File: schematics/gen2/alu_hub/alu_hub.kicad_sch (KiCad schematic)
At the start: 0 parts

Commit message: feat: alu hub + pcb base not finished yet
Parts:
- added BC1: BusConnector, Connector_PCBEdge:BUS_PCIexpress_x16, symbol cpu816symbols:BusConnector
- added C1, C10, C11, C2, C3, C4, C5, C6, C7, C8, C9: C, Capacitor_SMD:C_0805_2012Metric_Pad1.18x1.45mm_HandSolder, symbol Device:C
- added U1, U6: 74LS574, Package_DIP:DIP-20_W7.62mm_Socket_LongPads, symbol 74xx:74LS574
- added U10, U3, U9: 74LS02, Package_DIP:DIP-14_W7.62mm_Socket_LongPads, symbol 74xx:74LS02
- added U2, U7, U8: 74LS245, Package_DIP:DIP-20_W7.62mm_Socket_LongPads, symbol 74xx:74LS245
- added U4, U5: 74LS181, Package_DIP:DIP-24_W15.24mm_Socket_LongPads, symbol 74xx:74LS181
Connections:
- new net: U9.10, U9.11
- new net: U10.10, U9.12
- new net: U10.11, U10.12, U9.13
- new net: U3.4, U6.11 (Cp)
- new net: BC1.A20 (~{LARGL}), U3.5
- new net: BC1.B73 (~{CLK}), U3.3, U3.6
- new net: U10.1, U10.8
- new net: U10.4, U10.9
- new net: BC1.A62 (ALUSO), U5.13 (F3), U8.11 (B7), U9.6
- new net: U5.11 (F2), U8.12 (B6), U9.5
- new net: U5.10 (F1), U8.13 (B5), U9.3
- new net: U5.9 (F0), U8.14 (B4), U9.2
- new net: U10.6, U4.13 (F3), U8.15 (B3)
- new net: U10.5, U4.11 (F2), U8.16 (B2)
- new net: U10.3, U4.10 (F1), U8.17 (B1)
- new net: U10.2, U4.9 (F0), U8.18 (B0)
- new net: BC1.B30 (~{RALU}), U8.19 (CE)
- new net: U9.4, U9.9
- new net: BC1.B20 (~{RARGL}), U7.19 (CE)
- new net: BC1.A19 (~{LARGH}), U3.2
- new net: BC1.A60 (ALUZO), U10.13
- new net: BC1.A61 (~{ALUCO}), U5.16 (Cn+4)
- new net: BC1.B19 (~{RARGH}), U2.19 (CE)
- new net: BC1.B37 (ALUM), U4.8 (M), U5.8 (M)
- new net: BC1.B38 (~{ALUCI}), U4.7 (Cn)
- new net: BC1.B48 (ALUS0), U4.6 (S0), U5.6 (S0)
- new net: BC1.B49 (ALUS1), U4.5 (S1), U5.5 (S1)
- new net: BC1.B51 (ALUS2), U4.4 (S2), U5.4 (S2)
- new net: BC1.B52 (ALUS3), U4.3 (S3), U5.3 (S3)
- new net: U9.1, U9.8
- new net: U1.11 (Cp), U3.1
- new net: U4.16 (Cn+4), U5.7 (Cn)
- new net DATA0: BC1.A51 (DATA0), U1.2 (D0), U2.2 (A0), U6.2 (D0), U7.2 (A0), U8.2 (A0)
- new net DATA1: BC1.A52 (DATA1), U1.3 (D1), U2.3 (A1), U6.3 (D1), U7.3 (A1), U8.3 (A1)
- new net DATA2: BC1.A53 (DATA2), U1.4 (D2), U2.4 (A2), U6.4 (D2), U7.4 (A2), U8.4 (A2)
- new net DATA3: BC1.A54 (DATA3), U1.5 (D3), U2.5 (A3), U6.5 (D3), U7.5 (A3), U8.5 (A3)
- new net DATA4: BC1.A55 (DATA4), U1.6 (D4), U2.6 (A4), U6.6 (D4), U7.6 (A4), U8.6 (A4)
- new net DATA5: BC1.A56 (DATA5), U1.7 (D5), U2.7 (A5), U6.7 (D5), U7.7 (A5), U8.7 (A5)
- new net DATA6: BC1.A57 (DATA6), U1.8 (D6), U2.8 (A6), U6.8 (D6), U7.8 (A6), U8.8 (A6)
- new net DATA7: BC1.A58 (DATA7), U1.9 (D7), U2.9 (A7), U6.9 (D7), U7.9 (A7), U8.9 (A7)
- new net GND: BC1.A12 (GND), BC1.A13 (GND), BC1.A23 (GND), BC1.A32 (GND), BC1.A41 (GND), BC1.A50 (GND), BC1.A59 (GND), BC1.A63 (GND), BC1.A64 (GND), BC1.A65 (GND), BC1.A66 (GND), BC1.A70 (GND), BC1.A71 (GND), BC1.A72 (GND), BC1.A73 (GND), BC1.A74 (GND), BC1.A75 (GND), BC1.A76 (GND), BC1.B12 (GND), BC1.B13 (GND), BC1.B23 (GND), BC1.B32 (GND), BC1.B41 (GND), BC1.B50 (GND), BC1.B59 (GND), BC1.B62 (GND), BC1.B63 (GND), BC1.B64 (GND), BC1.B65 (GND), BC1.B66 (GND), BC1.B67 (GND), BC1.B68 (GND), BC1.B69 (GND), BC1.B70 (GND), BC1.B71 (GND), BC1.B72 (GND), BC1.B75 (GND), BC1.B76 (GND), C1.1, C10.1, C11.1, C2.1, C3.1, C4.1, C5.1, C6.1, C7.1, C8.1, C9.1, U1.1 (OE), U1.10 (GND), U10.7 (GND), U2.1 (A->B), U2.10 (GND), U3.7 (GND), U4.12 (GND), U5.12 (GND), U6.1 (OE), U6.10 (GND), U7.1 (A->B), U7.10 (GND), U8.1 (A->B), U8.10 (GND), U9.7 (GND)
- new net HIGH0: U1.19 (Q0), U2.18 (B0), U4.2 (A0)
- new net HIGH1: U1.18 (Q1), U2.17 (B1), U4.23 (A1)
- new net HIGH2: U1.17 (Q2), U2.16 (B2), U4.21 (A2)
- new net HIGH3: U1.16 (Q3), U2.15 (B3), U4.19 (A3)
- new net HIGH4: U1.15 (Q4), U2.14 (B4), U5.1 (B0)
- new net HIGH5: U1.14 (Q5), U2.13 (B5), U5.22 (B1)
- new net HIGH6: U1.13 (Q6), U2.12 (B6), U5.20 (B2)
- new net HIGH7: U1.12 (Q7), U2.11 (B7), U5.18 (B3)
- new net LOW0: U5.2 (A0), U6.19 (Q0), U7.18 (B0)
- new net LOW1: U5.23 (A1), U6.18 (Q1), U7.17 (B1)
- new net LOW2: U5.21 (A2), U6.17 (Q2), U7.16 (B2)
- new net LOW3: U5.19 (A3), U6.16 (Q3), U7.15 (B3)
- new net LOW4: U4.1 (B0), U6.15 (Q4), U7.14 (B4)
- new net LOW5: U4.22 (B1), U6.14 (Q5), U7.13 (B5)
- new net LOW6: U4.20 (B2), U6.13 (Q6), U7.12 (B6)
- new net LOW7: U4.18 (B3), U6.12 (Q7), U7.11 (B7)
- new net VCC: BC1.A1 (VCC), BC1.A2 (VCC), BC1.A3 (VCC), BC1.A4 (VCC), BC1.A5 (VCC), BC1.B1 (VCC), BC1.B2 (VCC), BC1.B3 (VCC), BC1.B4 (VCC), BC1.B5 (VCC), C1.2, C10.2, C11.2, C2.2, C3.2, C4.2, C5.2, C6.2, C7.2, C8.2, C9.2, U1.20 (VCC), U10.14 (VCC), U2.20 (VCC), U3.14 (VCC), U4.24 (VCC), U5.24 (VCC), U6.20 (VCC), U7.20 (VCC), U8.20 (VCC), U9.14 (VCC)
- no-connect marks 0 -> 81

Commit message: feat(alu): added vcc and gnd back plate
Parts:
- C1, C10, C2, C3, C4, C5, C6, C7, C8, C9: footprint Capacitor_SMD:C_0805_2012Metric_Pad1.18x1.45mm_HandSolder -> Capacitor_THT:C_Disc_D3.0mm_W1.6mm_P2.50mm
- C11: footprint Capacitor_SMD:C_0805_2012Metric_Pad1.18x1.45mm_HandSolder -> Capacitor_THT:C_Radial_D6.3mm_H5.0mm_P2.50mm
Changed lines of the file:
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@@
 			)
 		)
-		(property "Footprint" "Capacitor_SMD:C_0805_2012Metric_Pad1.18x1.45mm_HandSolder"
+		(property "Footprint" "Capacitor_THT:C_Disc_D3.0mm_W1.6mm_P2.50mm"
 			(at 262.89 106.9848 0)
 			(effects
@@
 			)
 		)
-		(property "Footprint" "Capacitor_SMD:C_0805_2012Metric_Pad1.18x1.45mm_HandSolder"
+		(property "Footprint" "Capacitor_THT:C_Disc_D3.0mm_W1.6mm_P2.50mm"
 			(at 267.97 52.3748 0)
 			(effects
@@
 			)
 		)
-		(property "Footprint" "Capacitor_SMD:C_0805_2012Metric_Pad1.18x1.45mm_HandSolder"
+		(property "Footprint" "Capacitor_THT:C_Disc_D3.0mm_W1.6mm_P2.50mm"
 			(at 210.82 261.9248 0)
 			(effects
@@
 			)
 		)
-		(property "Footprint" "Capacitor_SMD:C_0805_2012Metric_Pad1.18x1.45mm_HandSolder"
+		(property "Footprint" "Capacitor_THT:C_Disc_D3.0mm_W1.6mm_P2.50mm"
 			(at 223.52 52.3748 0)
 			(effects
@@
 			)
 		)
-		(property "Footprint" "Capacitor_SMD:C_0805_2012Metric_Pad1.18x1.45mm_HandSolder"
+		(property "Footprint" "Capacitor_THT:C_Disc_D3.0mm_W1.6mm_P2.50mm"
 			(at 167.64 260.6548 0)
 			(effects
@@
 			)
 		)
-		(property "Footprint" "Capacitor_SMD:C_0805_2012Metric_Pad1.18x1.45mm_HandSolder"
+		(property "Footprint" "Capacitor_THT:C_Radial_D6.3mm_H5.0mm_P2.50mm"
 			(at 59.69 52.3748 0)
 			(effects
@@
 			)
 		)
-		(property "Footprint" "Capacitor_SMD:C_0805_2012Metric_Pad1.18x1.45mm_HandSolder"
+		(property "Footprint" "Capacitor_THT:C_Disc_D3.0mm_W1.6mm_P2.50mm"
 			(at 119.38 260.6548 0)
 			(effects
@@
 			)
 		)
-		(property "Footprint" "Capacitor_SMD:C_0805_2012Metric_Pad1.18x1.45mm_HandSolder"
+		(property "Footprint" "Capacitor_THT:C_Disc_D3.0mm_W1.6mm_P2.50mm"
 			(at 115.57 52.3748 0)
 			(effects
@@
 			)
 		)
-		(property "Footprint" "Capacitor_SMD:C_0805_2012Metric_Pad1.18x1.45mm_HandSolder"
+		(property "Footprint" "Capacitor_THT:C_Disc_D3.0mm_W1.6mm_P2.50mm"
 			(at 162.56 52.3748 0)
 			(effects
@@
 			)
 		)
-		(property "Footprint" "Capacitor_SMD:C_0805_2012Metric_Pad1.18x1.45mm_HandSolder"
+		(property "Footprint" "Capacitor_THT:C_Disc_D3.0mm_W1.6mm_P2.50mm"
 			(at 158.75 103.1748 0)
 			(effects
@@
 			)
 		)
-		(property "Footprint" "Capacitor_SMD:C_0805_2012Metric_Pad1.18x1.45mm_HandSolder"
+		(property "Footprint" "Capacitor_THT:C_Disc_D3.0mm_W1.6mm_P2.50mm"
 			(at 361.95 109.5248 0)
 			(effects

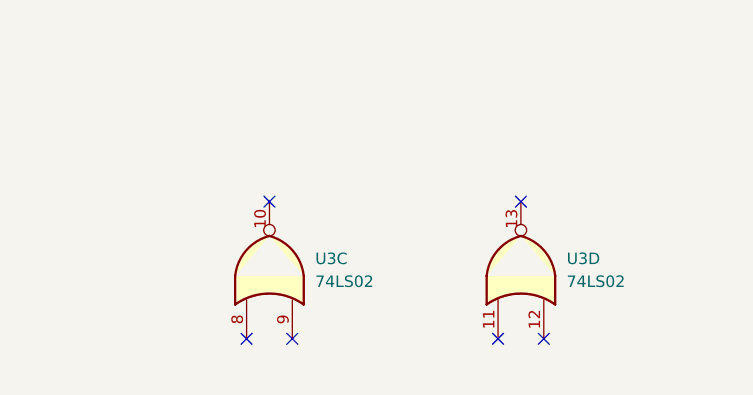
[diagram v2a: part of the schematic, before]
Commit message: feat(alu): add resistor symbol and connections to ALU hub schematic
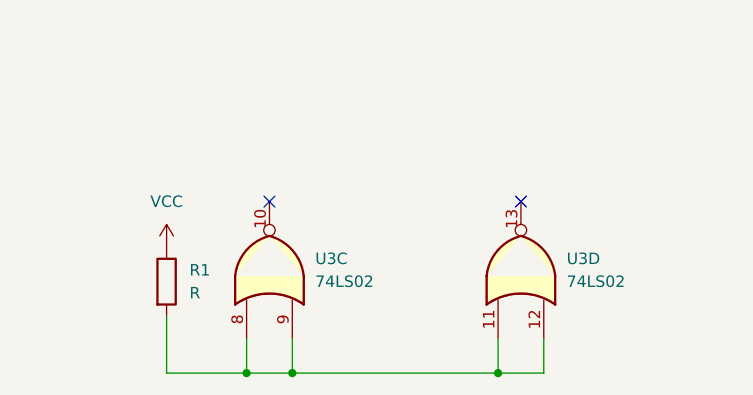
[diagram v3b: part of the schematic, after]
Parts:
- added R1: R, Resistor_THT:R_Axial_DIN0207_L6.3mm_D2.5mm_P7.62mm_Horizontal, symbol Device:R
- C4: footprint Capacitor_THT:C_Disc_D3.0mm_W1.6mm_P2.50mm -> C_Disc_D5.0mm_W2.5mm_P5.00mm
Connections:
- net VCC: now also R1.1
- net at U3.11: now also U3.12, U3.8, U3.9, R1.2
- no-connect marks 81 -> 77
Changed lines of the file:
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@@
 	)
 	(junction
+		(at 50.8 274.32)
+		(diameter 0)
+		(color 0 0 0 0)
+	)
+	(junction
 		(at 292.1 43.18)
 		(diameter 0)
@@
 	)
 	(junction
+		(at 78.74 274.32)
+		(diameter 0)
+		(color 0 0 0 0)
+	)
+	(junction
 		(at 142.24 147.32)
 		(diameter 0)
@@
 	)
 	(junction
+		(at 55.88 274.32)
+		(diameter 0)
+		(color 0 0 0 0)
+	)
+	(junction
 		(at 194.31 186.69)
 		(diameter 0)
@@
 	)
 	(no_connect
-		(at 55.88 270.51)
-	)
-	(no_connect
 		(at 44.45 127)
 	)
@@
 	)
 	(no_connect
-		(at 78.74 270.51)
-	)
-	(no_connect
 		(at 74.93 127)
 	)
@@
 	)
 	(no_connect
-		(at 50.8 270.51)
-	)
-	(no_connect
 		(at 74.93 163.83)
 	)
@@
 	)
 	(no_connect
-		(at 83.82 270.51)
-	)
-	(no_connect
 		(at 44.45 146.05)
 	)
@@
 	(wire
 		(pts
+			(xy 50.8 274.32) (xy 55.88 274.32)
+		)
+		(stroke
+			(width 0)
+			(type default)
+		)
+	)
+	(wire
+		(pts
 			(xy 173.99 127) (xy 189.23 127)
 		)
@@
 	(wire
 		(pts
+			(xy 55.88 270.51) (xy 55.88 274.32)
+		)
+		(stroke
+			(width 0)
+			(type default)
+		)
+	)
+	(wire
+		(pts
 			(xy 243.84 151.13) (xy 247.65 151.13)
 		)
@@
 		)
 	)
+	(wire
+		(pts
+			(xy 50.8 270.51) (xy 50.8 274.32)
+		)
+		(stroke
+			(width 0)
+			(type default)
+		)
+	)
 	(bus
 		(pts
@@
 	(wire
 		(pts
+			(xy 55.88 274.32) (xy 78.74 274.32)
+		)
+		(stroke
+			(width 0)
+			(type default)
+		)
+	)
+	(wire
+		(pts
 			(xy 115.57 52.07) (xy 115.57 53.34)
 		)
@@
 	(wire
 		(pts
+			(xy 78.74 274.32) (xy 83.82 274.32)
+		)
+		(stroke
+			(width 0)
+			(type default)
+		)
+	)
+	(wire
+		(pts
 			(xy 93.98 76.2) (xy 102.87 76.2)
 		)
@@
 	(wire
 		(pts
+			(xy 41.91 267.97) (xy 41.91 274.32)
+		)
+		(stroke
+			(width 0)
+			(type default)
+		)
+	)
+	(wire
+		(pts
 			(xy 299.72 133.35) (xy 349.25 133.35)
 		)
@@
 	(wire
 		(pts
+			(xy 83.82 270.51) (xy 83.82 274.32)
+		)
+		(stroke
+			(width 0)
+			(type default)
+		)
+	)
+	(wire
+		(pts
 			(xy 176.53 153.67) (xy 247.65 153.67)
 		)
@@
 	(wire
 		(pts
+			(xy 41.91 274.32) (xy 50.8 274.32)
+		)
+		(stroke
+			(width 0)
+			(type default)
+		)
+	)
+	(wire
+		(pts
 			(xy 283.21 95.25) (xy 302.26 95.25)
 		)
@@
 	(wire
 		(pts
+			(xy 78.74 270.51) (xy 78.74 274.32)
+		)
+		(stroke
+			(width 0)
+			(type default)
+		)
+	)
+	(wire
+		(pts
 			(xy 176.53 137.16) (xy 176.53 153.67)
 		)
@@
 	)
 	(symbol
+		(lib_id "Device:R")
+		(at 41.91 264.16 0)
+		(unit 1)
+		(exclude_from_sim no)
+		(in_bom yes)
+		(on_board yes)
+		(dnp no)
+		(fields_autoplaced yes)
+		(property "Reference" "R1"
+			(at 44.45 262.8899 0)
+			(effects
+				(font
+					(size 1.27 1.27)
+				)
+				(justify left)
+			)
+		)
+		(property "Value" "R"
+			(at 44.45 265.4299 0)
+			(effects
+				(font
+					(size 1.27 1.27)
+				)
+				(justify left)
+			)
+		)
+		(property "Footprint" "Resistor_THT:R_Axial_DIN0207_L6.3mm_D2.5mm_P7.62mm_Horizontal"
+			(at 40.132 264.16 90)
+			(effects
+				(font
+					(size 1.27 1.27)
+				)
+				(hide yes)
+			)
+		)
+		(property "Datasheet" "'"
+			(at 41.91 264.16 0)
+			(effects
+				(font
+					(size 1.27 1.27)
+				)
+				(hide yes)
+			)
+		)
+		(property "Description" "Resistor"
+			(at 41.91 264.16 0)
+			(effects
+				(font
+					(size 1.27 1.27)
+				)
+				(hide yes)
+			)
+		)
+		(pin "2"
+		)
+		(pin "1"
+		)
+		(instances
+			(project ""
+				(path "/63bf5833-673b-41a8-8365-6351cd154882"
+					(reference "R1")
+					(unit 1)
+				)
+			)
+		)
+	)
+	(symbol
 		(lib_id "power:GND")
 		(at 369.57 110.49 0)
@@
 	(symbol
 		(lib_id "power:VCC")
+		(at 41.91 260.35 0)
+		(unit 1)
+		(exclude_from_sim no)
+		(in_bom yes)
+		(on_board yes)
+		(dnp no)
+		(fields_autoplaced yes)
+		(property "Reference" "#PWR037"
+			(at 41.91 264.16 0)
+			(effects
+				(font
+					(size 1.27 1.27)
+				)
+				(hide yes)
+			)
+		)
+		(property "Value" "VCC"
+			(at 41.91 255.27 0)
+			(effects
+				(font
+					(size 1.27 1.27)
+				)
+			)
+		)
+		(property "Footprint" ""
+			(at 41.91 260.35 0)
+			(effects
+				(font
+					(size 1.27 1.27)
+				)
+				(hide yes)
+			)
+		)
+		(property "Datasheet" ""
+			(at 41.91 260.35 0)
+			(effects
+				(font
+					(size 1.27 1.27)
+				)
+				(hide yes)
+			)
+		)
+		(property "Description" "Power symbol creates a global label with name \"VCC\""
+			(at 41.91 260.35 0)
+			(effects
+				(font
+					(size 1.27 1.27)
+				)
+				(hide yes)
+			)
+		)
+		(pin "1"
+		)
+		(instances
+			(project ""
+				(path "/63bf5833-673b-41a8-8365-6351cd154882"
+					(reference "#PWR037")
+					(unit 1)
+				)
+			)
+		)
+	)
+	(symbol
+		(lib_id "power:VCC")
 		(at 115.57 52.07 0)
 		(unit 1)
@@
 			)
 		)
-		(property "Footprint" "Capacitor_THT:C_Disc_D3.0mm_W1.6mm_P2.50mm"
+		(property "Footprint" "C_Disc_D5.0mm_W2.5mm_P5.00mm"
 			(at 158.75 103.1748 0)
 			(effects

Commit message: alu hub done
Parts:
- C1, C10, C2, C3, C6, C7, C8, C9: footprint Capacitor_THT:C_Disc_D3.0mm_W1.6mm_P2.50mm -> Capacitor_THT:C_Disc_D5.0mm_W2.5mm_P5.00mm
- C4: footprint C_Disc_D5.0mm_W2.5mm_P5.00mm -> Capacitor_THT:C_Disc_D5.0mm_W2.5mm_P5.00mm
- C5: footprint Capacitor_THT:C_Disc_D3.0mm_W1.6mm_P2.50mm -> Capacitor_THT:C_Disc_D5.0mm_W2.5mm_P2.50mm
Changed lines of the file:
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@@
 			)
 		)
-		(property "Footprint" "Capacitor_THT:C_Disc_D3.0mm_W1.6mm_P2.50mm"
+		(property "Footprint" "Capacitor_THT:C_Disc_D5.0mm_W2.5mm_P5.00mm"
 			(at 262.89 106.9848 0)
 			(effects
@@
 			)
 		)
-		(property "Footprint" "Capacitor_THT:C_Disc_D3.0mm_W1.6mm_P2.50mm"
+		(property "Footprint" "Capacitor_THT:C_Disc_D5.0mm_W2.5mm_P5.00mm"
 			(at 267.97 52.3748 0)
 			(effects
@@
 			)
 		)
-		(property "Footprint" "Capacitor_THT:C_Disc_D3.0mm_W1.6mm_P2.50mm"
+		(property "Footprint" "Capacitor_THT:C_Disc_D5.0mm_W2.5mm_P5.00mm"
 			(at 210.82 261.9248 0)
 			(effects
@@
 			)
 		)
-		(property "Footprint" "Capacitor_THT:C_Disc_D3.0mm_W1.6mm_P2.50mm"
+		(property "Footprint" "Capacitor_THT:C_Disc_D5.0mm_W2.5mm_P2.50mm"
 			(at 223.52 52.3748 0)
 			(effects
@@
 			)
 		)
-		(property "Footprint" "Capacitor_THT:C_Disc_D3.0mm_W1.6mm_P2.50mm"
+		(property "Footprint" "Capacitor_THT:C_Disc_D5.0mm_W2.5mm_P5.00mm"
 			(at 167.64 260.6548 0)
 			(effects
@@
 			)
 		)
-		(property "Footprint" "Capacitor_THT:C_Disc_D3.0mm_W1.6mm_P2.50mm"
+		(property "Footprint" "Capacitor_THT:C_Disc_D5.0mm_W2.5mm_P5.00mm"
 			(at 119.38 260.6548 0)
 			(effects
@@
 			)
 		)
-		(property "Footprint" "Capacitor_THT:C_Disc_D3.0mm_W1.6mm_P2.50mm"
+		(property "Footprint" "Capacitor_THT:C_Disc_D5.0mm_W2.5mm_P5.00mm"
 			(at 115.57 52.3748 0)
 			(effects
@@
 			)
 		)
-		(property "Footprint" "Capacitor_THT:C_Disc_D3.0mm_W1.6mm_P2.50mm"
+		(property "Footprint" "Capacitor_THT:C_Disc_D5.0mm_W2.5mm_P5.00mm"
 			(at 162.56 52.3748 0)
 			(effects
@@
 			)
 		)
-		(property "Footprint" "C_Disc_D5.0mm_W2.5mm_P5.00mm"
+		(property "Footprint" "Capacitor_THT:C_Disc_D5.0mm_W2.5mm_P5.00mm"
 			(at 158.75 103.1748 0)
 			(effects
@@
 			)
 		)
-		(property "Footprint" "Capacitor_THT:C_Disc_D3.0mm_W1.6mm_P2.50mm"
+		(property "Footprint" "Capacitor_THT:C_Disc_D5.0mm_W2.5mm_P5.00mm"
 			(at 361.95 109.5248 0)
 			(effects
